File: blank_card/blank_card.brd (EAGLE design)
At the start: 100 x 80 mm, 1 part, among them J1 09231486921

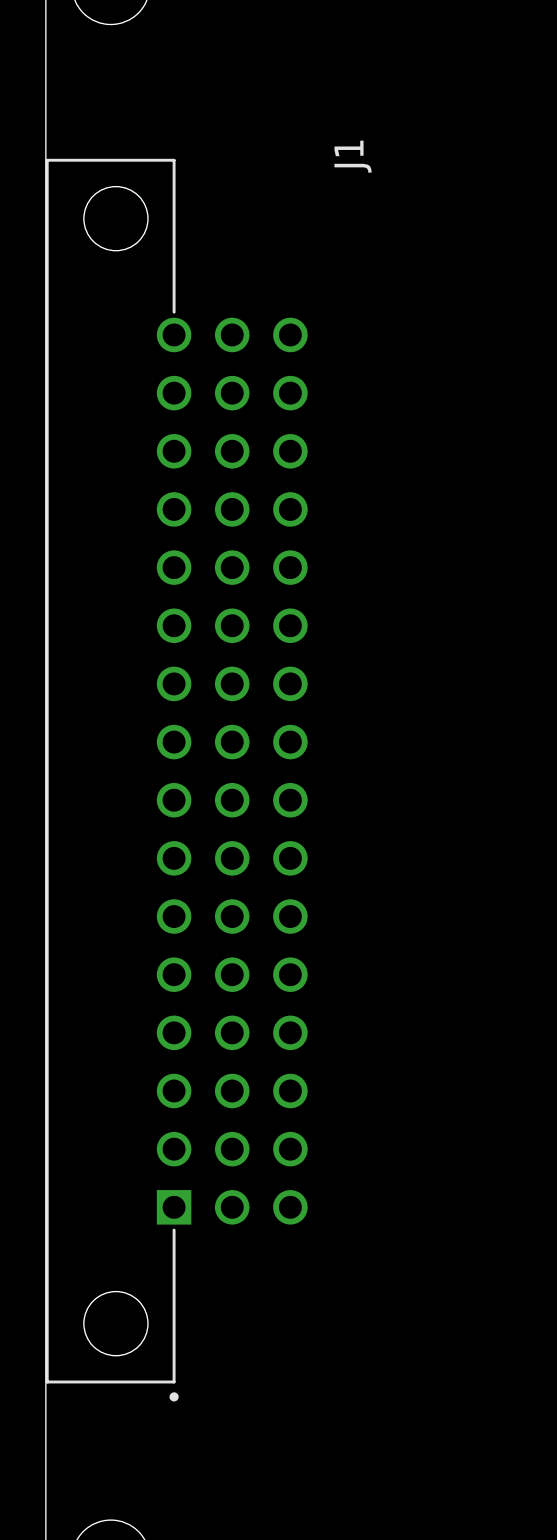
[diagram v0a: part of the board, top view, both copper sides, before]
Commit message: got rid of a 0.05mm offset in the position of the din41612 connectors
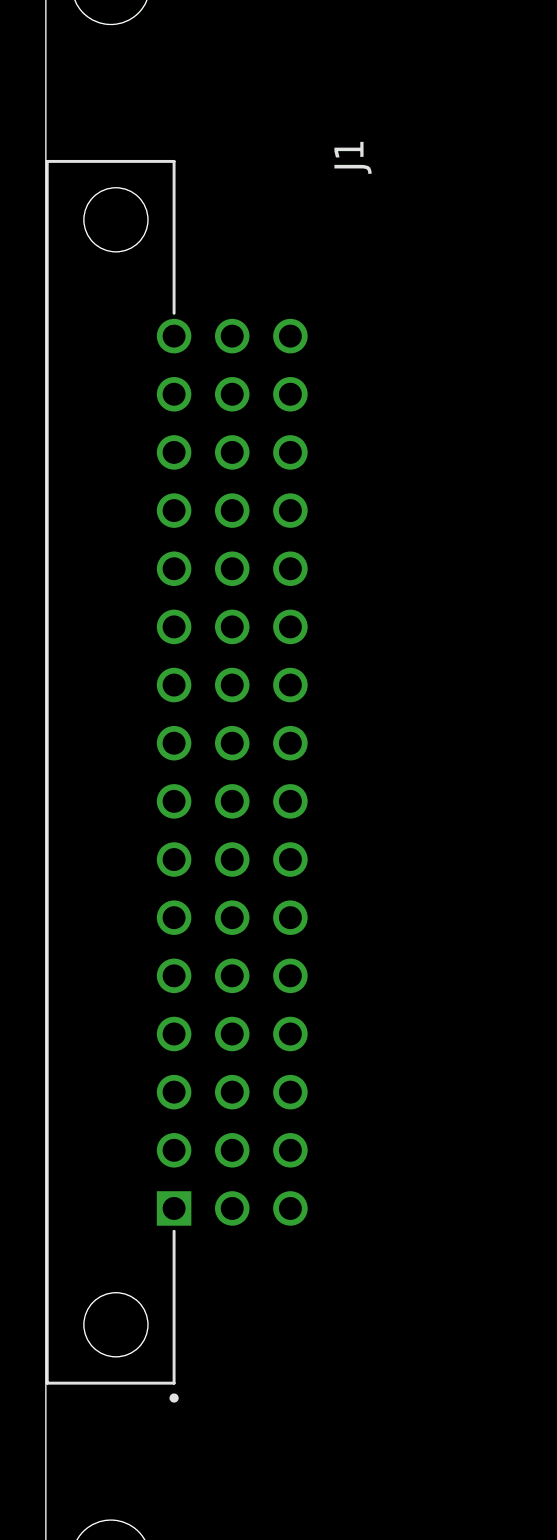
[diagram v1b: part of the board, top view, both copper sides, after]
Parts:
- moved J1 0.05 mm to (5.60, 20.9)
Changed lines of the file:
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@@
 </layers>
 <board>
-<fusionsync huburn="a.cGVyc29uYWw6dWUyYTJjODE0" projecturn="a.cGVyc29uYWw6dWUyYWFmMDMwIzIwMjAwODE1MzIzNjg3MzAx" f3durn="urn:adsk.wipprod:dm.lineage:NT6bbvTxRCGuvUQ9lO227A" pcbguid="c2abf58f-2678-4c4e-87e2-c47bafc57357" lastpulledtime="" lastsyncedchangeguid="" latestrevisionid="5d4b7890-4cdb-422a-9e05-c5c19d8ac431" lastsyncedrevisionid="5d4b7890-4cdb-422a-9e05-c5c19d8ac431" lastboardhashguid="67462d07-9d8e-1d45-e081-f3df2ff39551" lastpushedtime="2021-10-22T01:03:12Z" linktopcb3d="true"/>
+<fusionsync huburn="a.cGVyc29uYWw6dWUyYTJjODE0" projecturn="a.cGVyc29uYWw6dWUyYWFmMDMwIzIwMjAwODE1MzIzNjg3MzAx" f3durn="urn:adsk.wipprod:dm.lineage:NT6bbvTxRCGuvUQ9lO227A" pcbguid="" lastpulledtime="" lastsyncedchangeguid="" latestrevisionid="5d4b7890-4cdb-422a-9e05-c5c19d8ac431" lastsyncedrevisionid="5d4b7890-4cdb-422a-9e05-c5c19d8ac431" lastboardhashguid="67462d07-9d8e-1d45-e081-f3df2ff39551" lastpushedtime="2021-10-22T01:03:12Z" linktopcb3d="true"/>
 <plain>
 <wire x1="0" y1="0" x2="100" y2="0" width="0" layer="20"/>
@@
 </autorouter>
 <elements>
-<element name="J1" library="din41612_48_pin_board" package="HARTING_09231486921" value="09231486921" x="5.6" y="21" smashed="yes" rot="R270">
-<attribute name="AVAILABILITY" value="In Stock" x="5.6" y="21" size="1.778" layer="27" rot="R270" display="off"/>
-<attribute name="COMMENT" value="09231486921" x="5.6" y="21" size="1.778" layer="27" rot="R270" display="off"/>
-<attribute name="DESCRIPTION" value=" Conn DIN 41612 M 48 POS 2.54mm Solder RA Thru-Hole Tray " x="5.6" y="21" size="1.778" layer="27" rot="R270" display="off"/>
-<attribute name="EU_ROHS_COMPLIANCE" value="Compliant" x="5.6" y="21" size="1.778" layer="27" rot="R270" display="off"/>
-<attribute name="MF" value="HARTING" x="5.6" y="21" size="1.778" layer="27" rot="R270" display="off"/>
-<attribute name="MP" value="09231486921" x="5.6" y="21" size="1.778" layer="27" rot="R270" display="off"/>
-<attribute name="NAME" x="12.605" y="67.73" size="1.27" layer="25" rot="R270"/>
-<attribute name="PACKAGE" value="None" x="5.6" y="21" size="1.778" layer="27" rot="R270" display="off"/>
-<attribute name="PRICE" value="6$" x="5.6" y="21" size="1.778" layer="27" rot="R270" display="off"/>
-<attribute name="PURCHASE-URL-DIGIKEY" value="https://www.digikey.ca/en/products/detail/harting/09231486921/3180439" x="5.6" y="21" size="1.778" layer="27" rot="R270" display="off"/>
-<attribute name="VALUE" x="-8.59" y="67.73" size="1.27" layer="27" rot="R270"/>
+<element name="J1" library="din41612_48_pin_board" package="HARTING_09231486921" value="09231486921" x="5.6" y="20.95" smashed="yes" rot="R270">
+<attribute name="AVAILABILITY" value="In Stock" x="5.6" y="20.95" size="1.778" layer="27" rot="R270" display="off"/>
+<attribute name="COMMENT" value="09231486921" x="5.6" y="20.95" size="1.778" layer="27" rot="R270" display="off"/>
+<attribute name="DESCRIPTION" value=" Conn DIN 41612 M 48 POS 2.54mm Solder RA Thru-Hole Tray " x="5.6" y="20.95" size="1.778" layer="27" rot="R270" display="off"/>
+<attribute name="EU_ROHS_COMPLIANCE" value="Compliant" x="5.6" y="20.95" size="1.778" layer="27" rot="R270" display="off"/>
+<attribute name="MF" value="HARTING" x="5.6" y="20.95" size="1.778" layer="27" rot="R270" display="off"/>
+<attribute name="MP" value="09231486921" x="5.6" y="20.95" size="1.778" layer="27" rot="R270" display="off"/>
+<attribute name="NAME" x="12.605" y="67.68" size="1.27" layer="25" rot="R270"/>
+<attribute name="PACKAGE" value="None" x="5.6" y="20.95" size="1.778" layer="27" rot="R270" display="off"/>
+<attribute name="PRICE" value="6$" x="5.6" y="20.95" size="1.778" layer="27" rot="R270" display="off"/>
+<attribute name="PURCHASE-URL-DIGIKEY" value="https://www.digikey.ca/en/products/detail/harting/09231486921/3180439" x="5.6" y="20.95" size="1.778" layer="27" rot="R270" display="off"/>
+<attribute name="VALUE" x="-8.59" y="67.68" size="1.27" layer="27" rot="R270"/>
 </element>
 </elements>
@@
 <contactref element="J1" pad="18"/>
 <contactref element="J1" pad="19"/>
-<wire x1="10.68" y1="23.54" x2="10.68" y2="26.08" width="0" layer="19" extent="1-1"/>
-<wire x1="8.14" y1="26.08" x2="10.68" y2="26.08" width="0" layer="19" extent="1-1"/>
-<wire x1="5.6" y1="26.08" x2="8.14" y2="26.08" width="0" layer="19" extent="1-1"/>
-<wire x1="5.6" y1="28.62" x2="5.6" y2="26.08" width="0" layer="19" extent="1-1"/>
-<wire x1="10.68" y1="21" x2="10.68" y2="23.54" width="0" layer="19" extent="1-1"/>
-<wire x1="8.14" y1="23.54" x2="10.68" y2="23.54" width="0" layer="19" extent="1-1"/>
-<wire x1="5.6" y1="23.54" x2="5.6" y2="26.08" width="0" layer="19" extent="1-1"/>
-<wire x1="8.14" y1="21" x2="10.68" y2="21" width="0" layer="19" extent="1-1"/>
-<wire x1="5.6" y1="21" x2="5.6" y2="23.54" width="0" layer="19" extent="1-1"/>
+<wire x1="10.68" y1="23.49" x2="10.68" y2="26.03" width="0" layer="19" extent="1-1"/>
+<wire x1="8.14" y1="26.03" x2="10.68" y2="26.03" width="0" layer="19" extent="1-1"/>
+<wire x1="5.6" y1="26.03" x2="8.14" y2="26.03" width="0" layer="19" extent="1-1"/>
+<wire x1="5.6" y1="28.57" x2="5.6" y2="26.03" width="0" layer="19" extent="1-1"/>
+<wire x1="10.68" y1="20.95" x2="10.68" y2="23.49" width="0" layer="19" extent="1-1"/>
+<wire x1="8.14" y1="23.49" x2="10.68" y2="23.49" width="0" layer="19" extent="1-1"/>
+<wire x1="5.6" y1="23.49" x2="5.6" y2="26.03" width="0" layer="19" extent="1-1"/>
+<wire x1="8.14" y1="20.95" x2="10.68" y2="20.95" width="0" layer="19" extent="1-1"/>
+<wire x1="5.6" y1="20.95" x2="5.6" y2="23.49" width="0" layer="19" extent="1-1"/>
 </signal>
 <signal name="24V/12V" class="1">
@@
 <contactref element="J1" pad="21"/>
 <contactref element="J1" pad="22"/>
-<wire x1="10.68" y1="28.62" x2="10.68" y2="31.16" width="0" layer="19" extent="1-1"/>
-<wire x1="8.14" y1="31.16" x2="10.68" y2="31.16" width="0" layer="19" extent="1-1"/>
-<wire x1="8.14" y1="33.7" x2="8.14" y2="31.16" width="0" layer="19" extent="1-1"/>
-<wire x1="5.6" y1="33.7" x2="8.14" y2="33.7" width="0" layer="19" extent="1-1"/>
-<wire x1="5.6" y1="31.16" x2="8.14" y2="31.16" width="0" layer="19" extent="1-1"/>
-<wire x1="8.14" y1="28.62" x2="10.68" y2="28.62" width="0" layer="19" extent="1-1"/>
+<wire x1="10.68" y1="28.57" x2="10.68" y2="31.11" width="0" layer="19" extent="1-1"/>
+<wire x1="8.14" y1="31.11" x2="10.68" y2="31.11" width="0" layer="19" extent="1-1"/>
+<wire x1="8.14" y1="33.65" x2="8.14" y2="31.11" width="0" layer="19" extent="1-1"/>
+<wire x1="5.6" y1="33.65" x2="8.14" y2="33.65" width="0" layer="19" extent="1-1"/>
+<wire x1="5.6" y1="31.11" x2="8.14" y2="31.11" width="0" layer="19" extent="1-1"/>
+<wire x1="8.14" y1="28.57" x2="10.68" y2="28.57" width="0" layer="19" extent="1-1"/>
 </signal>
 <signal name="3.3V">
 <contactref element="J1" pad="7"/>
 <contactref element="J1" pad="23"/>
-<wire x1="5.6" y1="36.24" x2="8.14" y2="36.24" width="0" layer="19" extent="1-1"/>
+<wire x1="5.6" y1="36.19" x2="8.14" y2="36.19" width="0" layer="19" extent="1-1"/>
 </signal>
 <signal name="CS_1">
@@
 <contactref element="J1" pad="38"/>
 <contactref element="J1" pad="39"/>
-<wire x1="10.68" y1="33.7" x2="10.68" y2="36.24" width="0" layer="19" extent="1-1"/>
+<wire x1="10.68" y1="33.65" x2="10.68" y2="36.19" width="0" layer="19" extent="1-1"/>
 </signal>
 <signal name="SCK">
